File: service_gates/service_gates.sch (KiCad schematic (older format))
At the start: 1 part, among them P1 DIN_41612_128P

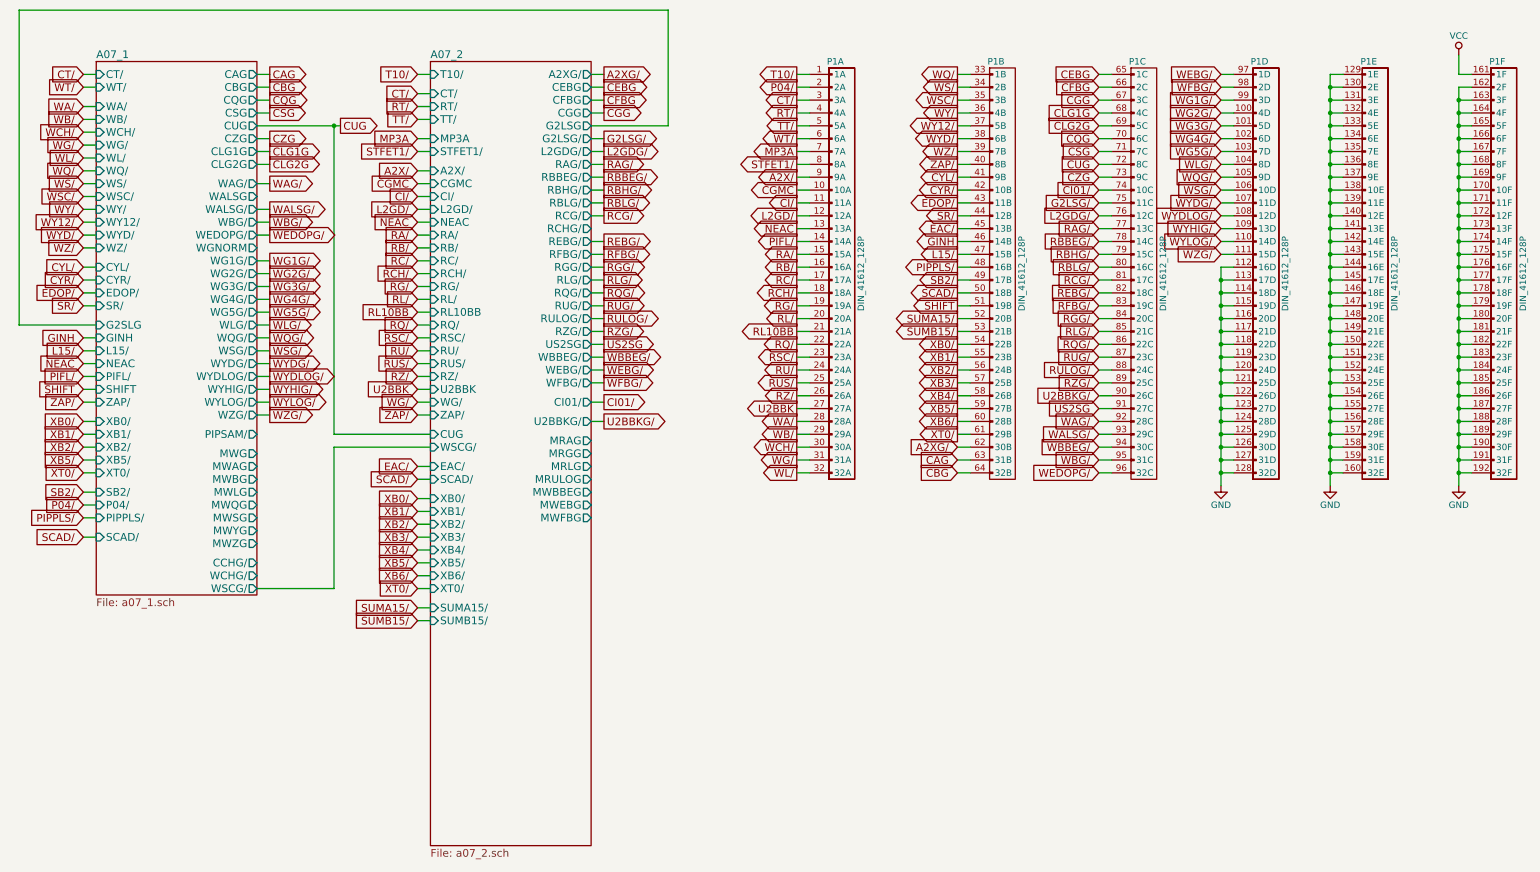
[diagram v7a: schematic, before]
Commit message: Tied in Inout IV and renamed MONPCH to the original MON+CH
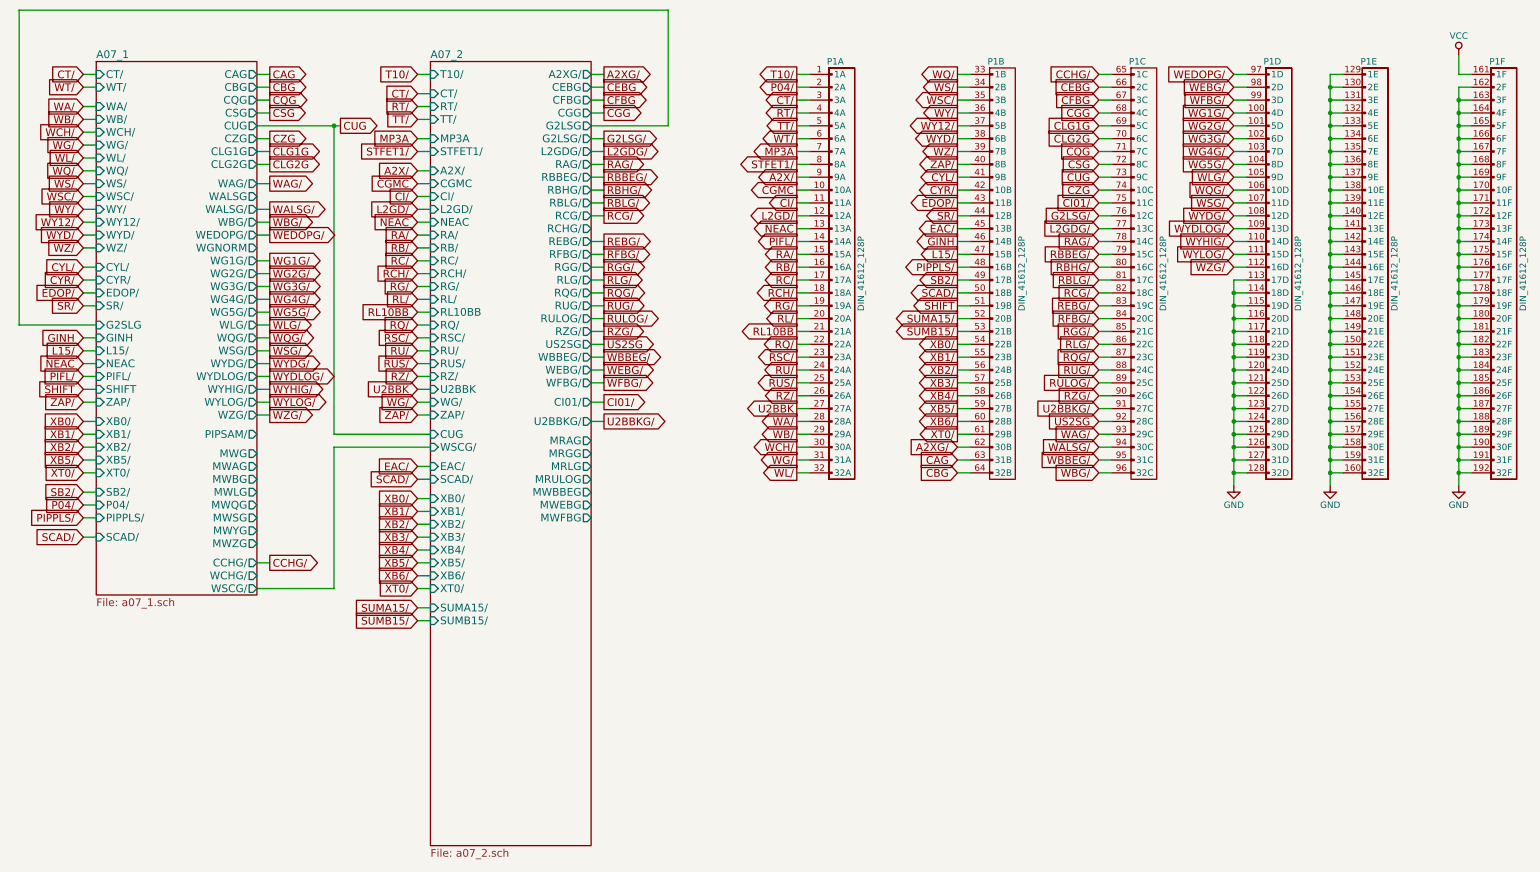
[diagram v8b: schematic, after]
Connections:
- net CEBG: now also P1.66 (2C); no longer P1.65 (1C)
- net CFBG: now also P1.67 (3C); no longer P1.66 (2C)
- net CGG: now also P1.68 (4C); no longer P1.67 (3C)
- net CI01/: now also P1.75 (11C); no longer P1.74 (10C)
- net CLG1G: now also P1.69 (5C); no longer P1.68 (4C)
- net CLG2G: now also P1.70 (6C); no longer P1.69 (5C)
- net CQG: now also P1.71 (7C); no longer P1.70 (6C)
- net CSG: now also P1.72 (8C); no longer P1.71 (7C)
- net CUG: now also P1.73 (9C); no longer P1.72 (8C)
- net CZG: now also P1.74 (10C); no longer P1.73 (9C)
- net G2LSG/: now also P1.76 (12C); no longer P1.75 (11C)
- net GND: no longer P1.112 (16D)
- net L2GDG/: now also P1.77 (13C); no longer P1.76 (12C)
- net RAG/: now also P1.78 (14C); no longer P1.77 (13C)
- net RBBEG/: now also P1.79 (15C); no longer P1.78 (14C)
- net RBHG/: now also P1.80 (16C); no longer P1.79 (15C)
- net RBLG/: now also P1.81 (17C); no longer P1.80 (16C)
- net RCG/: now also P1.82 (18C); no longer P1.81 (17C)
- net REBG/: now also P1.83 (19C); no longer P1.82 (18C)
- net RFBG/: now also P1.84 (20C); no longer P1.83 (19C)
- net RGG/: now also P1.85 (21C); no longer P1.84 (20C)
- net RLG/: now also P1.86 (22C); no longer P1.85 (21C)
- net RQG/: now also P1.87 (23C); no longer P1.86 (22C)
- net RUG/: now also P1.88 (24C); no longer P1.87 (23C)
- net RULOG/: now also P1.89 (25C); no longer P1.88 (24C)
- net RZG/: now also P1.90 (26C); no longer P1.89 (25C)
- net U2BBKG/: now also P1.91 (27C); no longer P1.90 (26C)
- net US2SG: now also P1.92 (28C); no longer P1.91 (27C)
- net WAG/: now also P1.93 (29C); no longer P1.92 (28C)
- net WALSG/: now also P1.94 (30C); no longer P1.93 (29C)
- net WBBEG/: now also P1.95 (31C); no longer P1.94 (30C)
- net WBG/: now also P1.96 (32C); no longer P1.95 (31C)
- net WEBG/: now also P1.98 (2D); no longer P1.97 (1D)
- net WEDOPG/: now also P1.97 (1D); no longer P1.96 (32C)
- net WFBG/: now also P1.99 (3D); no longer P1.98 (2D)
- net WG1G/: now also P1.100 (4D); no longer P1.99 (3D)
- net WG2G/: now also P1.101 (5D); no longer P1.100 (4D)
- net WG3G/: now also P1.102 (6D); no longer P1.101 (5D)
- net WG4G/: now also P1.103 (7D); no longer P1.102 (6D)
- net WG5G/: now also P1.104 (8D); no longer P1.103 (7D)
- net WLG/: now also P1.105 (9D); no longer P1.104 (8D)
- net WQG/: now also P1.106 (10D); no longer P1.105 (9D)
- net WSG/: now also P1.107 (11D); no longer P1.106 (10D)
- net WYDG/: now also P1.108 (12D); no longer P1.107 (11D)
- net WYDLOG/: now also P1.109 (13D); no longer P1.108 (12D)
- net WYHIG/: now also P1.110 (14D); no longer P1.109 (13D)
- net WYLOG/: now also P1.111 (15D); no longer P1.110 (14D)
- net WZG/: now also P1.112 (16D); no longer P1.111 (15D)
- new net CCHG/: P1.65 (1C)
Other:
- moved on the sheet: P1D
